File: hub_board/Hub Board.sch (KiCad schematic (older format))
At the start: 23 parts, among them J1 Conn_01x04, J2 Conn_01x04, J3 Conn_01x04, J4 Conn_01x04, P4 SERIAL, SW1 Switch_SPDT_x2, SW2 Switch_DPST, U0 10118194, U1 LM3671, U3 ESP-12E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

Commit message: Renamed files and cleaned up library links
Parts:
- U1: symbol LM3671-RESCUE-Coordinator_Board -> LM3671
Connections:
- wire segments 114 -> 143
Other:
- moved on the sheet: F0, L1, U0
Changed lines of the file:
@@
 EESchema Schematic File Version 2
+LIBS:diode
 LIBS:power
 LIBS:device
@@
 LIBS:logic_programmable
 LIBS:74xgxx
-LIBS:Coordinator Board-cache
+LIBS:Hub Board-cache
 EELAYER 25 0
 EELAYER END
@@
 $EndDescr
 $Comp
-L LM3671-RESCUE-Coordinator_Board U1
+L LM3671 U1
 U 1 1 57A0D83A
-P 2450 4800
-F 0 "U1" H 2200 5025 60  0000 L CNN
-F 1 "LM3671" H 2200 4550 60  0000 L CNN
-F 2 "TO_SOT_Packages_SMD:SOT-23-5" H 1950 3950 60  0000 C CNN
-F 3 "" H 2450 4450 60  0000 C CNN
-	1    2450 4800
+P 2500 4800
+F 0 "U1" H 2300 5050 60  0000 L CNN
+F 1 "LM3671" H 2250 4550 60  0000 L CNN
+F 2 "TO_SOT_Packages_SMD:SOT-23-5" H 2000 3950 60  0000 C CNN
+F 3 "" H 2500 4450 60  0000 C CNN
+	1    2500 4800
 	1    0    0    -1
 $EndComp
@@
 L INDUCTOR L1
 U 1 1 57A0E1B1
-P 3200 4700
-F 0 "L1" V 3150 4700 50  0000 C CNN
-F 1 "2.2uH" V 3300 4700 50  0000 C CNN
-F 2 "Resistors_SMD:R_0805_HandSoldering" V 3400 5000 50  0000 C CNN
-F 3 "" H 3200 4700 50  0000 C CNN
-	1    3200 4700
+P 3450 4700
+F 0 "L1" V 3400 4700 50  0000 C CNN
+F 1 "2.2uH" V 3550 4700 50  0000 C CNN
+F 2 "Resistors_SMD:R_0805_HandSoldering" V 3650 5000 50  0000 C CNN
+F 3 "" H 3450 4700 50  0000 C CNN
+	1    3450 4700
 	0    -1   -1   0
 $EndComp
@@
 L 10118194 U0
 U 1 1 5A5AABAF
-P 1000 4850
-F 0 "U0" H 900 5350 60  0000 C CNN
-F 1 "10118194" H 900 5150 60  0000 C CNN
-F 2 "nebrius-conn:10118194" H 1000 4850 60  0001 C CNN
-F 3 "" H 1000 4850 60  0001 C CNN
-	1    1000 4850
+P 1000 4900
+F 0 "U0" H 900 5400 60  0000 C CNN
+F 1 "10118194" H 900 5200 60  0000 C CNN
+F 2 "nebrius-conn:10118194" H 1000 4900 60  0001 C CNN
+F 3 "" H 1000 4900 60  0001 C CNN
+	1    1000 4900
 	0    -1   -1   0
 $EndComp
-NoConn ~ 1200 4850
-NoConn ~ 1200 4950
-NoConn ~ 1200 5050
+NoConn ~ 1200 4900
+NoConn ~ 1200 5000
+NoConn ~ 1200 5100
 NoConn ~ 2250 4050
 $Comp
@@
 L Fuse F0
 U 1 1 5A6BD755
-P 1450 5150
-F 0 "F0" V 1530 5150 50  0000 C CNN
-F 1 "Fuse" V 1375 5150 50  0000 C CNN
-F 2 "Resistors_SMD:R_0805_HandSoldering" V 1380 5150 50  0001 C CNN
-F 3 "" H 1450 5150 50  0001 C CNN
-	1    1450 5150
+P 1450 5200
+F 0 "F0" V 1530 5200 50  0000 C CNN
+F 1 "Fuse" V 1375 5200 50  0000 C CNN
+F 2 "Resistors_SMD:R_0805_HandSoldering" V 1380 5200 50  0001 C CNN
+F 3 "" H 1450 5200 50  0001 C CNN
+	1    1450 5200
 	0    1    1    0
 $EndComp
@@
 	2850 4150 3000 4150
 Wire Wire Line
-	2000 4350 2000 4800
-Wire Wire Line
 	2000 4700 2050 4700
 Connection ~ 2000 4700
 Wire Wire Line
-	1600 4900 2050 4900
-Wire Wire Line
-	1850 4750 1850 5250
-Connection ~ 1850 4900
-Wire Wire Line
-	2850 4700 2900 4700
-Wire Wire Line
-	3000 4350 3000 3800
-Wire Wire Line
-	1850 4350 3000 4350
+	1850 4750 1850 4800
+Wire Wire Line
+	1850 4800 1850 5250
+Wire Wire Line
+	2950 4700 3150 4700
+Wire Wire Line
+	3000 4350 3000 4150
+Wire Wire Line
+	3000 4150 3000 3800
+Wire Wire Line
+	1850 4350 2000 4350
+Wire Wire Line
+	2000 4350 3000 4350
 Wire Wire Line
 	1850 4350 1850 4450
 Connection ~ 2000 4350
 Wire Wire Line
-	3850 4600 3850 5050
-Wire Wire Line
-	2850 4900 3850 4900
+	3850 4600 3850 4700
+Wire Wire Line
+	3850 4700 3850 4900
+Wire Wire Line
+	3850 4900 3850 5050
+Wire Wire Line
+	2950 4900 3850 4900
 Connection ~ 3850 4900
 Wire Wire Line
-	2000 4800 2050 4800
-Wire Wire Line
-	3500 4700 3850 4700
+	3750 4700 3850 4700
 Connection ~ 3850 4700
 Wire Wire Line
@@
 	4550 4850 4550 5750
 Wire Wire Line
-	5100 4550 5750 4550
+	5100 4550 5650 4550
+Wire Wire Line
+	5650 4550 5750 4550
 Wire Wire Line
 	5650 4150 5650 4550
@@
 	5300 3250 5300 3350
 Wire Wire Line
-	1600 4900 1600 4750
-Wire Wire Line
-	1600 4750 1200 4750
+	1600 4800 1200 4800
 Connection ~ 3000 4150
 Wire Wire Line
 	2250 4250 1700 4250
 Wire Wire Line
-	1700 4250 1700 5150
+	1700 4250 1700 5200
 Wire Wire Line
 	3000 1450 3000 1350
 Wire Wire Line
-	2650 1450 4950 1450
+	2650 1450 3000 1450
+Wire Wire Line
+	3000 1450 3650 1450
+Wire Wire Line
+	3650 1450 4300 1450
+Wire Wire Line
+	4300 1450 4950 1450
 Wire Wire Line
 	2650 1450 2650 1350
@@
 Connection ~ 3650 1450
 Wire Wire Line
-	5250 1350 5250 1650
+	5250 1350 5250 1550
+Wire Wire Line
+	5250 1550 5250 1650
 Wire Wire Line
 	3950 1550 3950 1350
@@
 Connection ~ 3950 1550
 Wire Wire Line
-	5950 1850 5950 2600
+	5950 1850 5950 1950
+Wire Wire Line
+	5950 1950 5950 2600
 Wire Wire Line
 	5950 1950 6050 1950
@@
 Connection ~ 5950 1950
 Wire Wire Line
-	7250 1850 7250 2600
+	7250 1850 7250 1950
+Wire Wire Line
+	7250 1950 7250 2600
 Wire Wire Line
 	7250 1950 7150 1950
@@
 	7150 2050 7350 2050
 Wire Wire Line
-	7350 2050 7350 2900
+	7350 2050 7350 2700
+Wire Wire Line
+	7350 2700 7350 2900
 Wire Wire Line
 	7150 2700 7350 2700
@@
 	6050 2050 5850 2050
 Wire Wire Line
-	5850 2050 5850 2900
+	5850 2050 5850 2700
+Wire Wire Line
+	5850 2700 5850 2900
 Wire Wire Line
 	6050 2700 5850 2700
 Connection ~ 5850 2700
 Wire Wire Line
-	3200 2150 6050 2150
-Wire Wire Line
-	3100 2800 6050 2800
-Wire Wire Line
-	1200 5150 1300 5150
-Wire Wire Line
-	1700 5150 1600 5150
+	3200 2150 3850 2150
+Wire Wire Line
+	3850 2150 4500 2150
+Wire Wire Line
+	4500 2150 5150 2150
+Wire Wire Line
+	5150 2150 6050 2150
+Wire Wire Line
+	3100 2800 3750 2800
+Wire Wire Line
+	3750 2800 4400 2800
+Wire Wire Line
+	4400 2800 5050 2800
+Wire Wire Line
+	5050 2800 6050 2800
+Wire Wire Line
+	1200 5200 1300 5200
+Wire Wire Line
+	1700 5200 1600 5200
 Wire Wire Line
 	7750 2150 7750 4350
@@
 NoConn ~ 6400 3750
 Wire Wire Line
-	5200 4350 5200 6150
+	5200 4350 5200 5750
+Wire Wire Line
+	5200 5750 5200 6150
 $Comp
 L SF303GJ26 U5
@@
 $EndComp
 Wire Wire Line
-	5400 6550 5400 6750
+	5400 6550 5400 6650
+Wire Wire Line
+	5400 6650 5400 6750
 Wire Wire Line
 	5300 6550 5300 6650
@@
 	5750 4650 5300 4650
 Wire Wire Line
-	5300 4650 5300 6150
+	5300 4650 5300 5500
+Wire Wire Line
+	5300 5500 5300 6150
 Wire Wire Line
 	5750 4750 5400 4750
 Wire Wire Line
-	5400 4750 5400 6150
+	5400 4750 5400 5650
+Wire Wire Line
+	5400 5650 5400 6150
 Wire Wire Line
 	6600 5750 6800 5750
@@
 	7650 4450 7650 5400
 Wire Wire Line
-	5200 6650 5400 6650
+	5200 6650 5300 6650
+Wire Wire Line
+	5300 6650 5400 6650
 Wire Wire Line
 	5500 6550 5500 6650
@@
 	7550 4850 8850 4850
 Wire Wire Line
-	3300 1550 5250 1550
+	3300 1550 3950 1550
+Wire Wire Line
+	3950 1550 4600 1550
+Wire Wire Line
+	4600 1550 5250 1550
 $Comp
 L Conn_01x04 J3
@@
 Wire Wire Line
 	7150 2800 7850 2800
+Wire Wire Line
+	1600 4800 1850 4800
+Wire Wire Line
+	1850 4800 2050 4800
+Connection ~ 1850 4800
+Wire Wire Line
+	1600 4800 1600 4800
+Wire Wire Line
+	2000 4900 2050 4900
+Wire Wire Line
+	2000 4350 2000 4700
+Wire Wire Line
+	2000 4700 2000 4900
 $EndSCHEMATC

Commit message: Forgot to add unsaved changes
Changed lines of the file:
@@
 Connection ~ 2000 4700
 Wire Wire Line
-	1850 4750 1850 4800
-Wire Wire Line
-	1850 4800 1850 5250
+	1850 4750 1850 5250
 Wire Wire Line
 	2950 4700 3150 4700
 Wire Wire Line
-	3000 4350 3000 4150
-Wire Wire Line
-	3000 4150 3000 3800
-Wire Wire Line
-	1850 4350 2000 4350
-Wire Wire Line
-	2000 4350 3000 4350
+	3000 4350 3000 3800
+Wire Wire Line
+	1850 4350 3000 4350
 Wire Wire Line
 	1850 4350 1850 4450
 Connection ~ 2000 4350
 Wire Wire Line
-	3850 4600 3850 4700
-Wire Wire Line
-	3850 4700 3850 4900
-Wire Wire Line
-	3850 4900 3850 5050
+	3850 4600 3850 5050
 Wire Wire Line
 	2950 4900 3850 4900
@@
 	4550 4850 4550 5750
 Wire Wire Line
-	5100 4550 5650 4550
-Wire Wire Line
-	5650 4550 5750 4550
+	5100 4550 5750 4550
 Wire Wire Line
 	5650 4150 5650 4550
@@
 	5300 3250 5300 3350
 Wire Wire Line
-	1600 4800 1200 4800
+	1200 4800 2050 4800
 Connection ~ 3000 4150
 Wire Wire Line
@@
 	3000 1450 3000 1350
 Wire Wire Line
-	2650 1450 3000 1450
-Wire Wire Line
-	3000 1450 3650 1450
-Wire Wire Line
-	3650 1450 4300 1450
-Wire Wire Line
-	4300 1450 4950 1450
+	2650 1450 4950 1450
 Wire Wire Line
 	2650 1450 2650 1350
@@
 Connection ~ 3650 1450
 Wire Wire Line
-	5250 1350 5250 1550
-Wire Wire Line
-	5250 1550 5250 1650
+	5250 1350 5250 1650
 Wire Wire Line
 	3950 1550 3950 1350
@@
 Connection ~ 3950 1550
 Wire Wire Line
-	5950 1850 5950 1950
-Wire Wire Line
-	5950 1950 5950 2600
+	5950 1850 5950 2600
 Wire Wire Line
 	5950 1950 6050 1950
@@
 Connection ~ 5950 1950
 Wire Wire Line
-	7250 1850 7250 1950
-Wire Wire Line
-	7250 1950 7250 2600
+	7250 1850 7250 2600
 Wire Wire Line
 	7250 1950 7150 1950
@@
 	7150 2050 7350 2050
 Wire Wire Line
-	7350 2050 7350 2700
-Wire Wire Line
-	7350 2700 7350 2900
+	7350 2050 7350 2900
 Wire Wire Line
 	7150 2700 7350 2700
@@
 	6050 2050 5850 2050
 Wire Wire Line
-	5850 2050 5850 2700
-Wire Wire Line
-	5850 2700 5850 2900
+	5850 2050 5850 2900
 Wire Wire Line
 	6050 2700 5850 2700
 Connection ~ 5850 2700
 Wire Wire Line
-	3200 2150 3850 2150
-Wire Wire Line
-	3850 2150 4500 2150
-Wire Wire Line
-	4500 2150 5150 2150
-Wire Wire Line
-	5150 2150 6050 2150
-Wire Wire Line
-	3100 2800 3750 2800
-Wire Wire Line
-	3750 2800 4400 2800
-Wire Wire Line
-	4400 2800 5050 2800
-Wire Wire Line
-	5050 2800 6050 2800
+	3200 2150 6050 2150
+Wire Wire Line
+	3100 2800 6050 2800
 Wire Wire Line
 	1200 5200 1300 5200
@@
 NoConn ~ 6400 3750
 Wire Wire Line
-	5200 4350 5200 5750
-Wire Wire Line
-	5200 5750 5200 6150
+	5200 4350 5200 6150
 $Comp
 L SF303GJ26 U5
@@
 $EndComp
 Wire Wire Line
-	5400 6550 5400 6650
-Wire Wire Line
-	5400 6650 5400 6750
+	5400 6550 5400 6750
 Wire Wire Line
 	5300 6550 5300 6650
@@
 	5750 4650 5300 4650
 Wire Wire Line
-	5300 4650 5300 5500
-Wire Wire Line
-	5300 5500 5300 6150
+	5300 4650 5300 6150
 Wire Wire Line
 	5750 4750 5400 4750
 Wire Wire Line
-	5400 4750 5400 5650
-Wire Wire Line
-	5400 5650 5400 6150
+	5400 4750 5400 6150
 Wire Wire Line
 	6600 5750 6800 5750
@@
 	7650 4450 7650 5400
 Wire Wire Line
-	5200 6650 5300 6650
-Wire Wire Line
-	5300 6650 5400 6650
+	5200 6650 5400 6650
 Wire Wire Line
 	5500 6550 5500 6650
@@
 	7550 4850 8850 4850
 Wire Wire Line
-	3300 1550 3950 1550
-Wire Wire Line
-	3950 1550 4600 1550
-Wire Wire Line
-	4600 1550 5250 1550
+	3300 1550 5250 1550
 $Comp
 L Conn_01x04 J3
@@
 Wire Wire Line
 	7150 2800 7850 2800
-Wire Wire Line
-	1600 4800 1850 4800
-Wire Wire Line
-	1850 4800 2050 4800
 Connection ~ 1850 4800
 Wire Wire Line
@@
 	2000 4900 2050 4900
 Wire Wire Line
-	2000 4350 2000 4700
-Wire Wire Line
-	2000 4700 2000 4900
+	2000 4350 2000 4900
 $EndSCHEMATC

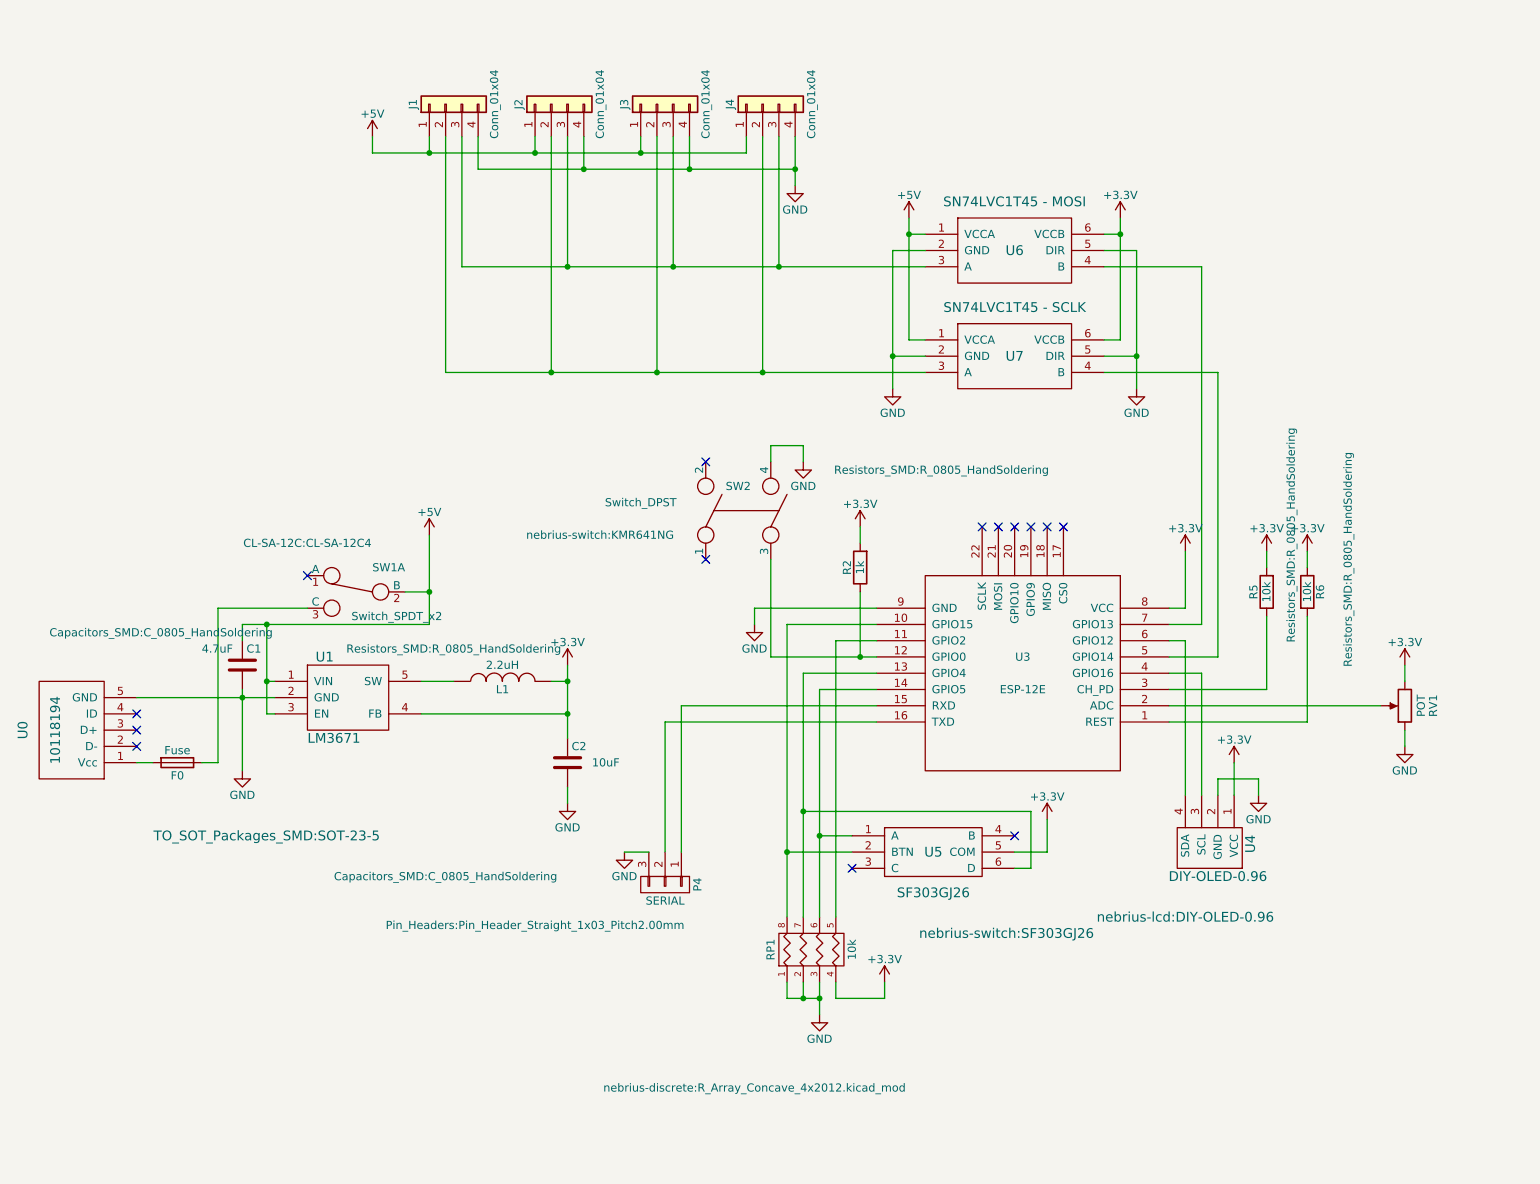
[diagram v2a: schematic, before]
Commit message: Updated and reverted a whole bunch of changes to use more tried-and-true connections
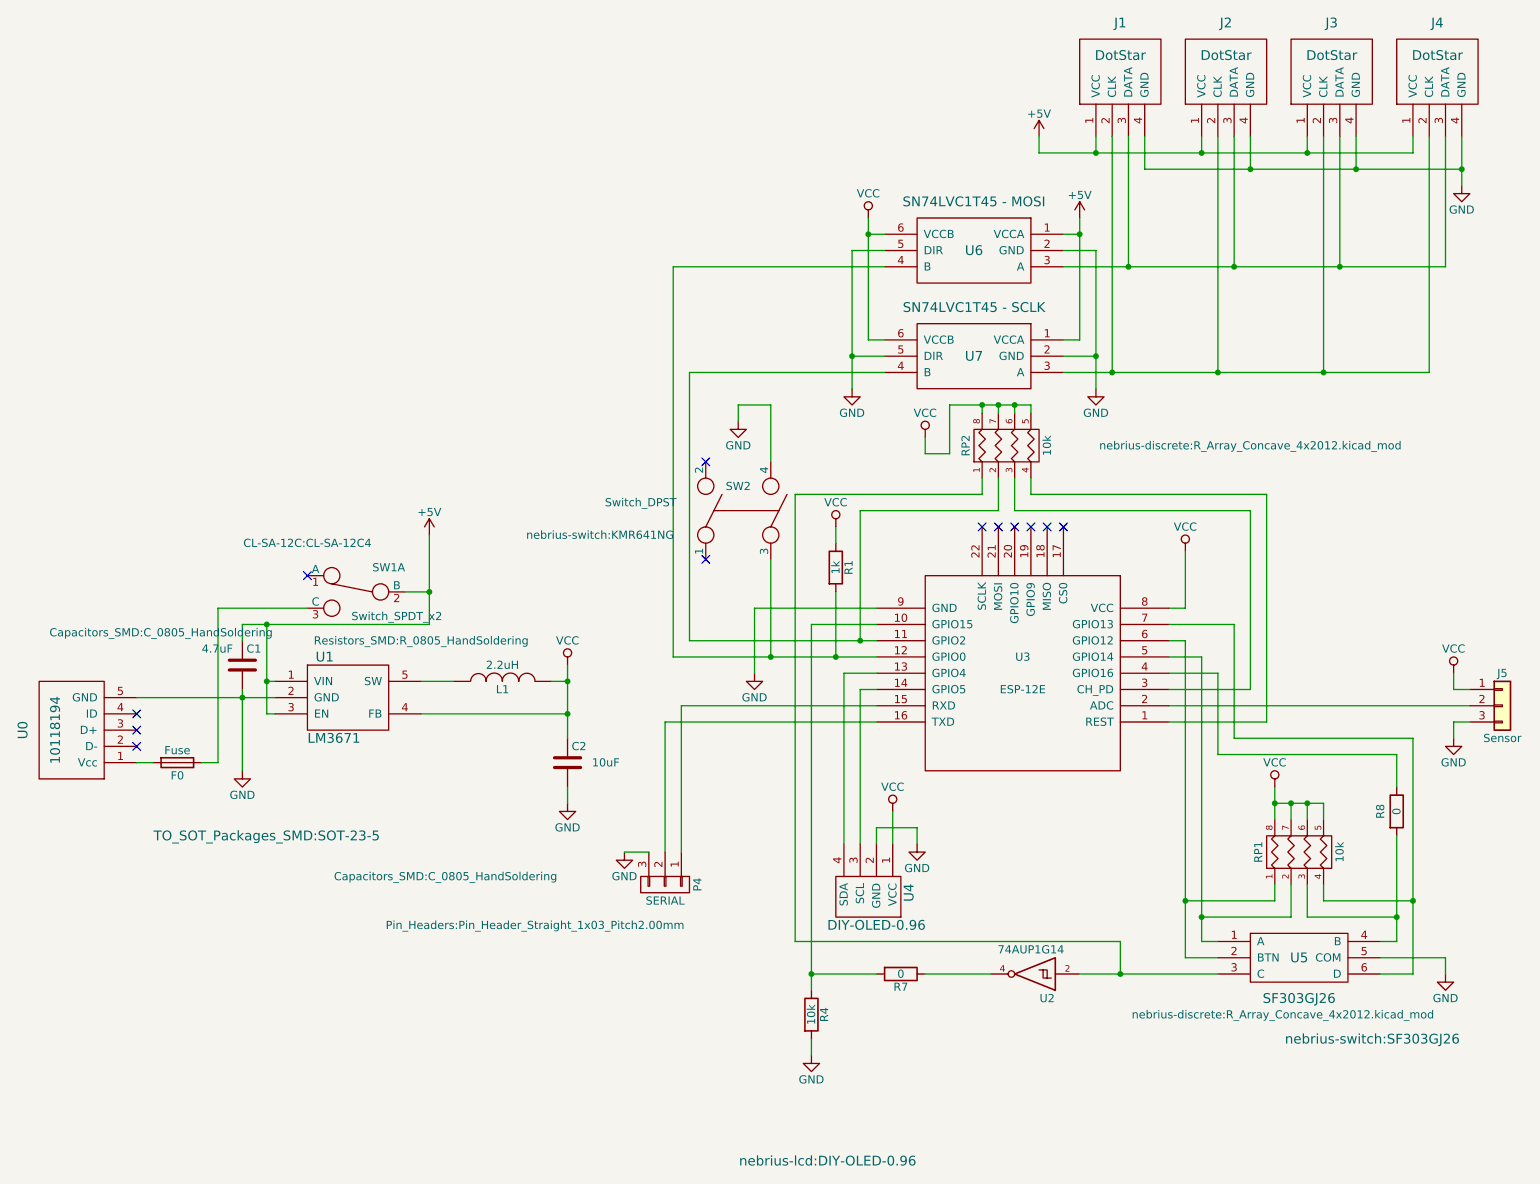
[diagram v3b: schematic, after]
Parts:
- removed J1, J2, J3, J4: Conn_01x04, Pin_Headers:Pin_Header_Angled_1x04_Pitch2.54mm, symbol Conn_01x04
- removed R2: 1k, Resistors_SMD:R_0805_HandSoldering, symbol R
- removed R5, R6: 10k, Resistors_SMD:R_0805_HandSoldering, symbol R
- removed RV1: POT, nebrius-discrete:Model-35-Pot, symbol POT
- added J1, J2, J3, J4: DotStar, Pin_Headers:Pin_Header_Angled_1x04_Pitch2.54mm, symbol DotStar
- added J5: Sensor, Pin_Headers:Pin_Header_Straight_1x03_Pitch2.00mm, symbol Conn_01x03
- added R1: 1k, Resistors_SMD:R_0805_HandSoldering, symbol R
- added R4: 10k, Resistors_SMD:R_0805_HandSoldering, symbol R
- added R7, R8: 0, Resistors_SMD:R_0805_HandSoldering, symbol R
- added RP2: 10k, nebrius-discrete:R_Array_Concave_4x2012.kicad_mod, symbol R_PACK4
- added U2: 74AUP1G14, TO_SOT_Packages_SMD:SOT-23-5_HandSoldering, symbol 74AUP1G14
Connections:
- net +5V: now also J1.1 (VCC), J2.1 (VCC), J3.1 (VCC), J4.1 (VCC)
- net GND: now also U5.5 (COM), J1.4 (GND), J2.4 (GND), J3.4 (GND), J4.4 (GND), J5.3 (Pin_3), R4.2, U2.3 (GND); no longer RP1.1 (P1), RP1.2 (P2), RP1.3 (P3)
- net at U3.1 (REST): now also RP2.4 (P4)
- net at U3.11 (GPIO2): now also U7.4 (B), RP2.2 (P2); no longer RP1.5 (R4)
- net at SW2.3, U3.12 (GPIO0): now also U6.4 (B), R1.2
- net at U3.2 (ADC): now also J5.2 (Pin_2)
- net at U3.3 (CH_PD): now also RP2.3 (P3)
- net at U4.3 (SCL): now also U3.14 (GPIO5); no longer U3.4 (GPIO16)
- net at U3.5 (GPIO14): now also RP1.2 (P2), U5.1 (A); no longer U7.4 (B)
- net at U4.4 (SDA): now also U3.13 (GPIO4); no longer U3.6 (GPIO12)
- net at U3.7 (GPIO13): now also RP1.4 (P4), U5.6 (D); no longer U6.4 (B)
- net at U5.3 (C): now also RP2.1 (P1), U2.2
- net at U5.4 (B): now also RP1.3 (P3), R8.2
- net at U7.3 (A): now also J1.2 (CLK), J2.2 (CLK), J3.2 (CLK), J4.2 (CLK)
- net at U6.3 (A): now also J1.3 (DATA), J2.3 (DATA), J3.3 (DATA), J4.3 (DATA)
- net +3V3 renamed VCC
- net VCC: now also RP1.5 (R4), RP1.6 (R3), RP1.7 (R2), RP1.8 (R1), J5.1 (Pin_1), R1.1, RP2.5 (R4), RP2.6 (R3), RP2.7 (R2), RP2.8 (R1), U2.5 (VCC); no longer RP1.4 (P4), U5.5 (COM)
- new net: R4.1, R7.2, U3.10 (GPIO15)
- new net: R8.1, U3.4 (GPIO16)
- new net: RP1.1 (P1), U3.6 (GPIO12), U5.2 (BTN)
- new net: R7.1, U2.4
- no-connect marks 14 -> 12
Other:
- moved on the sheet: RP1, U4, U5, U6, U7

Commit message: First steps in merging the endpoint and hub code
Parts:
- U1: footprint TO_SOT_Packages_SMD:SOT-23-5 -> TO_SOT_Packages_SMD:SOT-23-5_HandSoldering
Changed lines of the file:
@@
 F 0 "U1" H 2300 5050 60  0000 L CNN
 F 1 "LM3671" H 2250 4550 60  0000 L CNN
-F 2 "TO_SOT_Packages_SMD:SOT-23-5" H 2000 3950 60  0000 C CNN
+F 2 "TO_SOT_Packages_SMD:SOT-23-5_HandSoldering" H 2000 3950 60  0000 C CNN
 F 3 "" H 2500 4450 60  0000 C CNN
 	1    2500 4800
